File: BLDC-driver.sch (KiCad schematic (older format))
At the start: 103 parts, among them J1 Conn_01x06, J2 Conn_01x06, Q1 FDMS8018, Q2 FDMS8018, Q3 FDMS8018, Q4 FDMS8018, Q5 FDMS8018, Q6 FDMS8018, Q7 BC807, U1 NCP81151B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

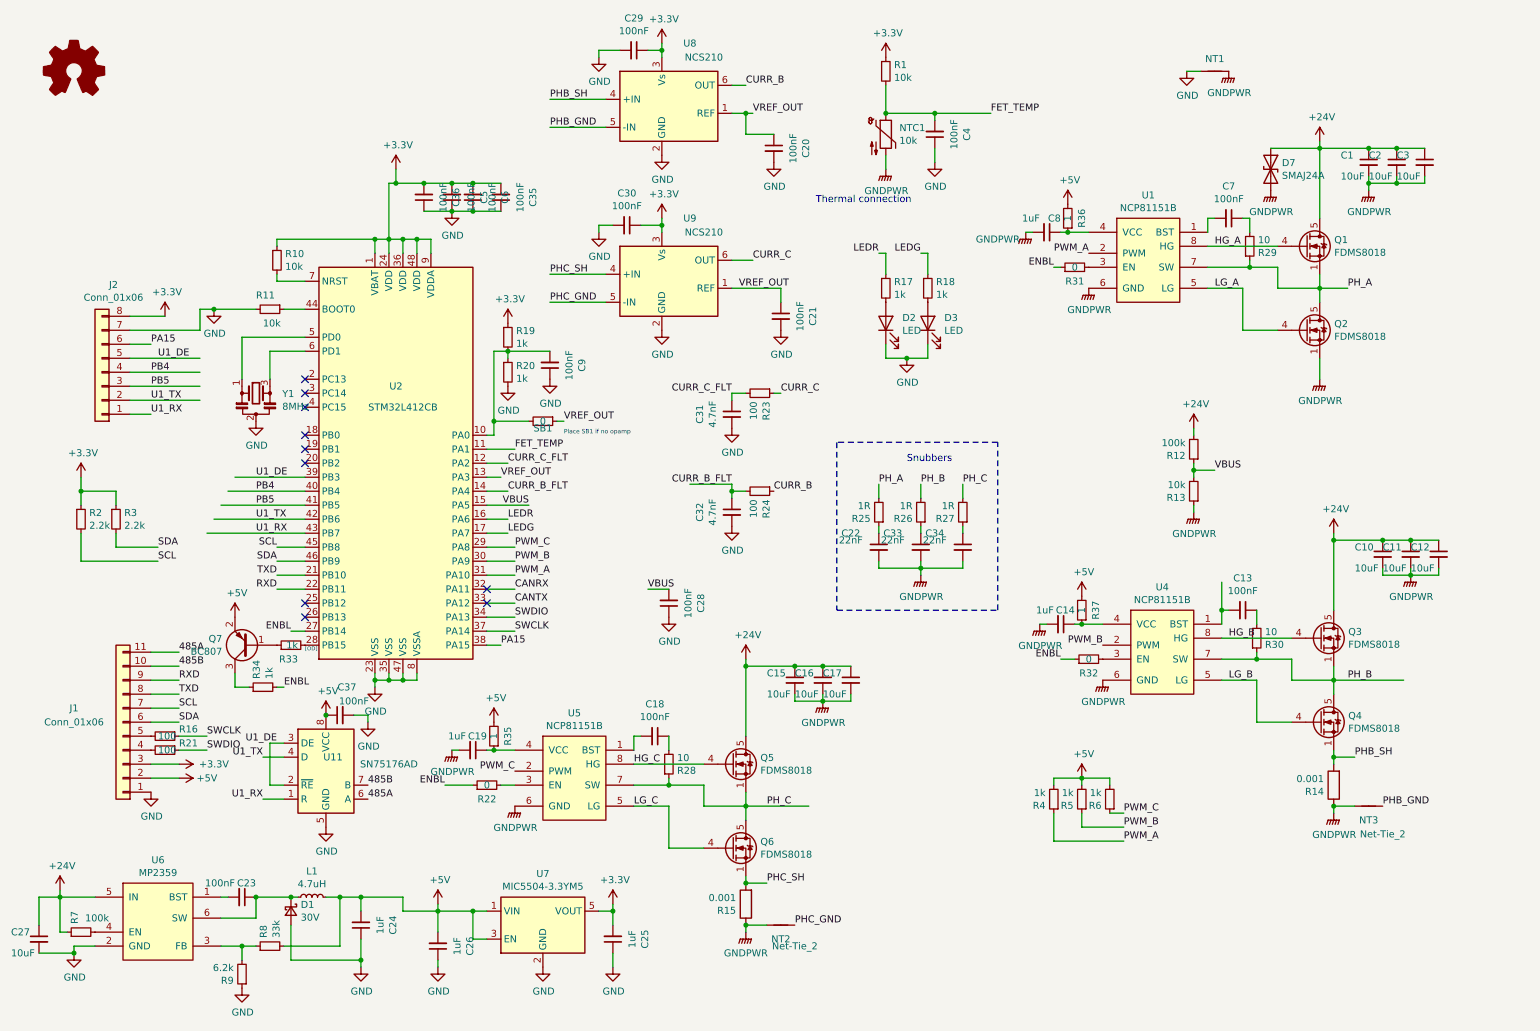
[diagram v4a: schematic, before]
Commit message: Multiple updates:
Change amp filter caps to 1nF
Move second shunt resistor to top layer
Make one hole grounded
various routing updates
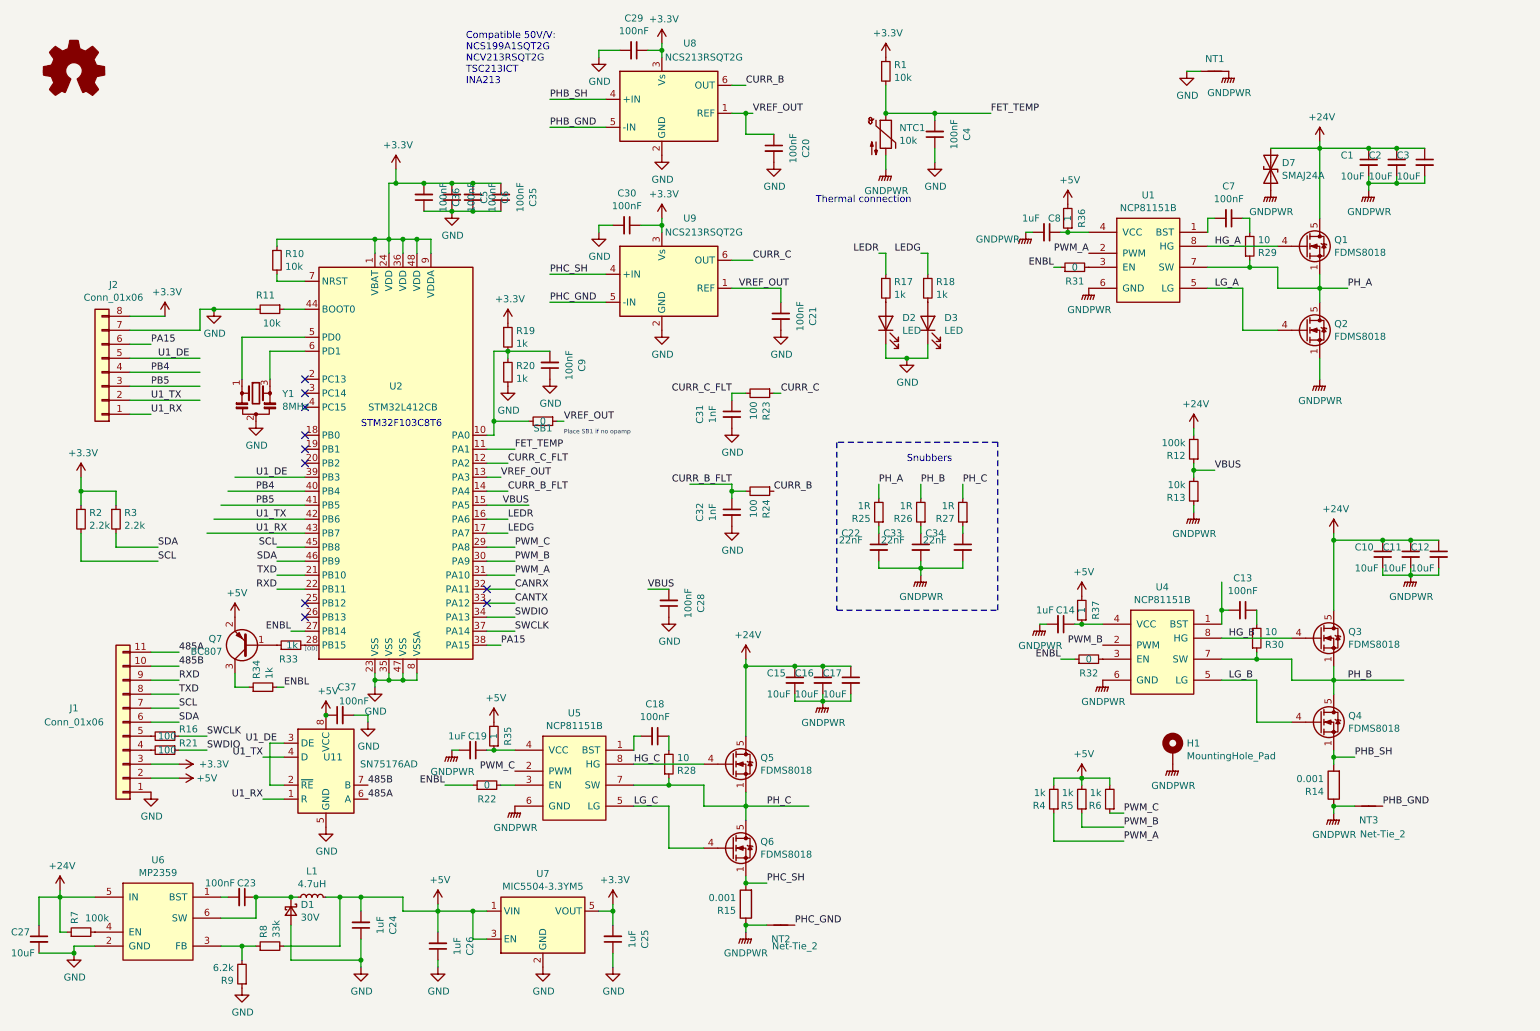
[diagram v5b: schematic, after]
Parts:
- added H1: MountingHole_Pad, MountingHole:MountingHole_3.2mm_M3_DIN965_Pad, symbol Mechanical:MountingHole_Pad
- C31, C32: value 4.7nF -> 1nF; JLCSMT C1538 -> C1523
- R14, R15: JLCSMT (none) -> C154629; JLCSMT_PKG (none) -> RES-SMD
- SB1: JLCSMT (none) -> C17168; JLCSMT_PKG (none) -> 0402
- U8, U9: value NCS210 -> NCS213RSQT2G
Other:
- note added: "Compatible 50V/V:\nNCS199A1SQT2G\nNCV213RSQT2G\nTSC213ICT\nINA213"
- note added: "STM32F103C8T6"
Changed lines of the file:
@@
 P 5100 1250
 F 0 "U8" H 5300 1750 50  0000 C CNN
-F 1 "NCS210" H 5400 1650 50  0000 C CNN
+F 1 "NCS213RSQT2G" H 5400 1650 50  0000 C CNN
 F 2 "Package_TO_SOT_SMD:SOT-363_SC-70-6" H 5100 1250 50  0001 C CNN
 F 3 "https://www.onsemi.com/pub/Collateral/NCS210R-D.PDF" H 5100 1250 50  0001 C CNN
@@
 F 4 "PMR25HZPFV1L00" H 9900 6050 50  0001 C CNN "MPN"
 F 5 "https://lt.farnell.com/rohm/pmr25hzpfv1l00/current-sense-res-0r001-1-1-w/dp/2696414" H 9900 6050 50  0001 C CNN "URL"
+F 6 "C154629" H 9900 6050 50  0001 C CNN "JLCSMT"
+F 7 "RES-SMD" H 9900 6050 50  0001 C CNN "JLCSMT_PKG"
 	1    9900 6050
 	-1   0    0    1
@@
 F 4 "PMR25HZPFV1L00" H 5700 6900 50  0001 C CNN "MPN"
 F 5 "https://lt.farnell.com/rohm/pmr25hzpfv1l00/current-sense-res-0r001-1-1-w/dp/2696414" H 5700 6900 50  0001 C CNN "URL"
+F 6 "C154629" H 5700 6900 50  0001 C CNN "JLCSMT"
+F 7 "RES-SMD" H 5700 6900 50  0001 C CNN "JLCSMT_PKG"
 	1    5700 6900
 	-1   0    0    1
@@
 P 5600 3400
 F 0 "C31" V 5371 3400 50  0000 C CNN
-F 1 "4.7nF" V 5462 3400 50  0000 C CNN
+F 1 "1nF" V 5462 3400 50  0000 C CNN
 F 2 "Capacitor_SMD:C_0402_1005Metric" H 5600 3400 50  0001 C CNN
 F 3 "~" H 5600 3400 50  0001 C CNN
-F 4 "C1538" H 5600 3400 50  0001 C CNN "JLCSMT"
+F 4 "C1523" H 5600 3400 50  0001 C CNN "JLCSMT"
 F 5 "0402" H 5600 3400 50  0001 C CNN "JLCSMT_PKG"
 	1    5600 3400
@@
 P 5600 4100
 F 0 "C32" V 5371 4100 50  0000 C CNN
-F 1 "4.7nF" V 5462 4100 50  0000 C CNN
+F 1 "1nF" V 5462 4100 50  0000 C CNN
 F 2 "Capacitor_SMD:C_0402_1005Metric" H 5600 4100 50  0001 C CNN
 F 3 "~" H 5600 4100 50  0001 C CNN
-F 4 "C1538" H 5600 4100 50  0001 C CNN "JLCSMT"
+F 4 "C1523" H 5600 4100 50  0001 C CNN "JLCSMT"
 F 5 "0402" H 5600 4100 50  0001 C CNN "JLCSMT_PKG"
 	1    5600 4100
@@
 P 5100 2500
 F 0 "U9" H 5300 3000 50  0000 C CNN
-F 1 "NCS210" H 5400 2900 50  0000 C CNN
+F 1 "NCS213RSQT2G" H 5400 2900 50  0000 C CNN
 F 2 "Package_TO_SOT_SMD:SOT-363_SC-70-6" H 5100 2500 50  0001 C CNN
 F 3 "https://www.onsemi.com/pub/Collateral/NCS210R-D.PDF" H 5100 2500 50  0001 C CNN
@@
 F 2 "Resistor_SMD:R_0402_1005Metric" H 4250 3450 50  0001 C CNN
 F 3 "~" H 4250 3450 50  0001 C CNN
+F 4 "C17168" H 4250 3450 50  0001 C CNN "JLCSMT"
+F 5 "0402" H 4250 3450 50  0001 C CNN "JLCSMT_PKG"
 	1    4250 3450
 	0    1    1    0
@@
 NoConn ~ 2550 4750
 NoConn ~ 2550 4850
+Text Notes 3700 1050 0    50   ~ 0
+Compatible 50V/V:\nNCS199A1SQT2G\nNCV213RSQT2G\nTSC213ICT\nINA213
+Text Notes 2950 3500 0    50   ~ 0
+STM32F103C8T6
+$Comp
+L Mechanical:MountingHole_Pad H1
+U 1 1 60F815C2
+P 8750 5800
+F 0 "H1" H 8850 5849 50  0000 L CNN
+F 1 "MountingHole_Pad" H 8850 5758 50  0000 L CNN
+F 2 "MountingHole:MountingHole_3.2mm_M3_DIN965_Pad" H 8750 5800 50  0001 C CNN
+F 3 "~" H 8750 5800 50  0001 C CNN
+	1    8750 5800
+	1    0    0    -1
+$EndComp
+$Comp
+L power:GNDPWR #PWR0130
+U 1 1 60F81DE6
+P 8750 5900
+F 0 "#PWR0130" H 8750 5700 50  0001 C CNN
+F 1 "GNDPWR" H 8754 5746 50  0000 C CNN
+F 2 "" H 8750 5850 50  0001 C CNN
+F 3 "" H 8750 5850 50  0001 C CNN
+	1    8750 5900
+	1    0    0    -1
+$EndComp
 $EndSCHEMATC

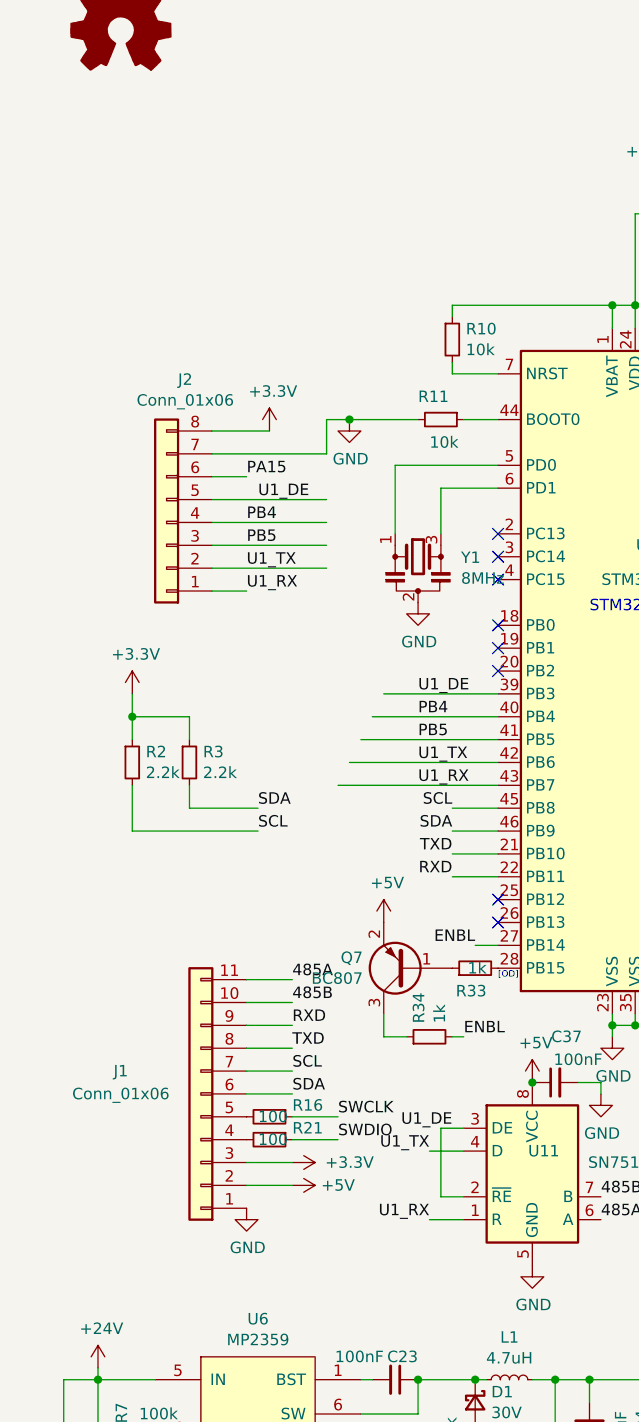
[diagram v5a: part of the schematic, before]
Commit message: Rev3: Update connectors, add JST PH connectors
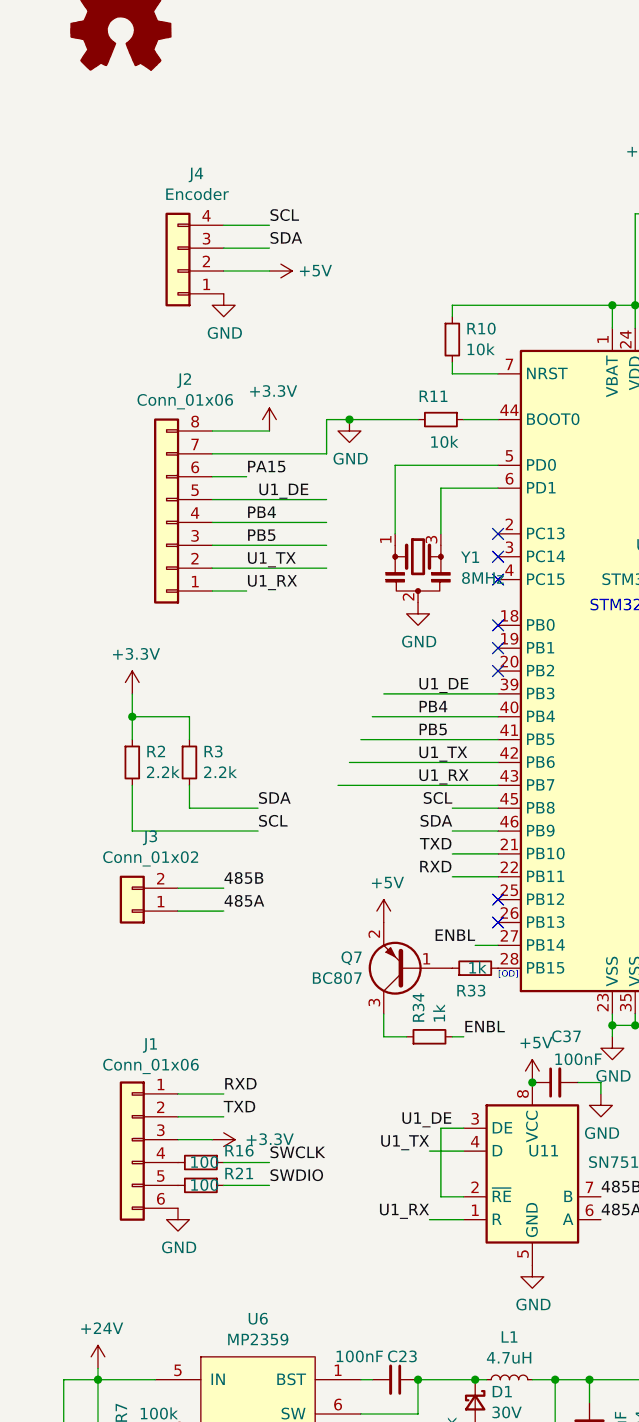
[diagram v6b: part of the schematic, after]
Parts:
- removed J1: Conn_01x06, Connector_PinHeader_2.00mm:PinHeader_1x11_P2.00mm_Vertical, symbol Connector_Generic:Conn_01x11
- added J1: Conn_01x06, Connector_JST:JST_PH_S6B-PH-K_1x06_P2.00mm_Horizontal, symbol Connector_Generic:Conn_01x06
- added J3: Conn_01x02, Connector_JST:JST_PH_S2B-PH-K_1x02_P2.00mm_Horizontal, symbol Connector_Generic:Conn_01x02
- added J4: Encoder, Connector_PinSocket_2.00mm:PinSocket_1x04_P2.00mm_Vertical, symbol Connector_Generic:Conn_01x04
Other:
- moved on the sheet: R16, R21
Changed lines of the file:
@@
 Wire Wire Line
 	3850 3550 3900 3550
-Text Label 1650 5300 0    50   ~ 0
+Text Label 1350 5600 0    50   ~ 0
 RXD
-Text Label 1650 5400 0    50   ~ 0
+Text Label 1350 5700 0    50   ~ 0
 TXD
 Wire Wire Line
-	1650 5400 1450 5400
-Wire Wire Line
-	1450 5300 1650 5300
-Text Label 1650 5500 0    50   ~ 0
+	1350 5700 1150 5700
+Wire Wire Line
+	1150 5600 1350 5600
+Text Label 1550 1800 0    50   ~ 0
 SCL
-Text Label 1650 5600 0    50   ~ 0
+Text Label 1550 1900 0    50   ~ 0
 SDA
 Wire Wire Line
-	1650 5500 1450 5500
-Wire Wire Line
-	1450 5600 1650 5600
-Text Label 1850 5700 0    50   ~ 0
+	1550 1800 1350 1800
+Wire Wire Line
+	1350 1900 1550 1900
+Text Label 1550 5900 0    50   ~ 0
 SWCLK
-Text Label 1850 5800 0    50   ~ 0
+Text Label 1550 6000 0    50   ~ 0
 SWDIO
 Wire Wire Line
-	1850 5700 1650 5700
-Wire Wire Line
-	1650 5800 1850 5800
+	1550 5900 1350 5900
 $Comp
 L power:GND #PWR034
 U 1 1 5F120A4B
-P 1450 6100
-F 0 "#PWR034" H 1450 5850 50  0001 C CNN
-F 1 "GND" H 1455 5927 50  0000 C CNN
-F 2 "" H 1450 6100 50  0001 C CNN
-F 3 "" H 1450 6100 50  0001 C CNN
-	1    1450 6100
+P 1150 6100
+F 0 "#PWR034" H 1150 5850 50  0001 C CNN
+F 1 "GND" H 1155 5927 50  0000 C CNN
+F 2 "" H 1150 6100 50  0001 C CNN
+F 3 "" H 1150 6100 50  0001 C CNN
+	1    1150 6100
 	1    0    0    -1
 $EndComp
@@
 L power:+5V #PWR032
 U 1 1 5EEDF35F
-P 1650 6000
-F 0 "#PWR032" H 1650 5850 50  0001 C CNN
-F 1 "+5V" V 1650 6200 50  0000 C CNN
-F 2 "" H 1650 6000 50  0001 C CNN
-F 3 "" H 1650 6000 50  0001 C CNN
-	1    1650 6000
+P 1550 2000
+F 0 "#PWR032" H 1550 1850 50  0001 C CNN
+F 1 "+5V" V 1550 2200 50  0000 C CNN
+F 2 "" H 1550 2000 50  0001 C CNN
+F 3 "" H 1550 2000 50  0001 C CNN
+	1    1550 2000
 	0    1    1    0
 $EndComp
 Wire Wire Line
-	1650 6000 1450 6000
+	1550 2000 1350 2000
 $Comp
 L power:GND #PWR046
@@
 L power:+3.3V #PWR0109
 U 1 1 5F9E74A9
-P 1650 5900
-F 0 "#PWR0109" H 1650 5750 50  0001 C CNN
-F 1 "+3.3V" V 1650 6150 50  0000 C CNN
-F 2 "" H 1650 5900 50  0001 C CNN
-F 3 "" H 1650 5900 50  0001 C CNN
-	1    1650 5900
+P 1300 5800
+F 0 "#PWR0109" H 1300 5650 50  0001 C CNN
+F 1 "+3.3V" V 1300 6050 50  0000 C CNN
+F 2 "" H 1300 5800 50  0001 C CNN
+F 3 "" H 1300 5800 50  0001 C CNN
+	1    1300 5800
 	0    1    1    0
 $EndComp
-Wire Wire Line
-	1650 5900 1450 5900
-Text Label 1650 5100 0    50   ~ 0
+Text Label 1350 4800 0    50   ~ 0
 485A
 Wire Wire Line
-	1650 5100 1450 5100
-Text Label 1650 5200 0    50   ~ 0
+	1350 4800 1150 4800
+Text Label 1350 4700 0    50   ~ 0
 485B
 Wire Wire Line
-	1650 5200 1450 5200
+	1350 4700 1150 4700
 Text Notes 6200 1900 0    50   ~ 0
 Thermal connection
@@
 $EndComp
 $Comp
-L Connector_Generic:Conn_01x11 J1
-U 1 1 5F108F52
-P 1250 5600
-F 0 "J1" H 1600 5500 50  0000 C CNN
-F 1 "Conn_01x06" H 1600 5600 50  0000 C CNN
-F 2 "Connector_PinHeader_2.00mm:PinHeader_1x11_P2.00mm_Vertical" H 1250 5600 50  0001 C CNN
-F 3 "~" H 1250 5600 50  0001 C CNN
-	1    1250 5600
-	-1   0    0    1
-$EndComp
-$Comp
 L Regulator_Linear:MIC5504-3.3YM5 U7
 U 1 1 5EEEC834
@@
 L Device:R_Small R16
 U 1 1 60B85EAE
-P 1550 5700
-F 0 "R16" V 1500 5800 50  0000 L CNN
-F 1 "100" V 1550 5650 50  0000 L CNN
-F 2 "Resistor_SMD:R_0402_1005Metric" H 1550 5700 50  0001 C CNN
-F 3 "~" H 1550 5700 50  0001 C CNN
-F 4 "0402" H 1550 5700 50  0001 C CNN "JLCSMT_PKG"
-F 5 "C25076" H 1550 5700 50  0001 C CNN "JLCSMT"
-	1    1550 5700
+P 1250 5900
+F 0 "R16" V 1200 6000 50  0000 L CNN
+F 1 "100" V 1250 5850 50  0000 L CNN
+F 2 "Resistor_SMD:R_0402_1005Metric" H 1250 5900 50  0001 C CNN
+F 3 "~" H 1250 5900 50  0001 C CNN
+F 4 "0402" H 1250 5900 50  0001 C CNN "JLCSMT_PKG"
+F 5 "C25076" H 1250 5900 50  0001 C CNN "JLCSMT"
+	1    1250 5900
 	0    1    1    0
 $EndComp
@@
 L Device:R_Small R21
 U 1 1 60BC204F
-P 1550 5800
-F 0 "R21" V 1500 5900 50  0000 L CNN
-F 1 "100" V 1550 5750 50  0000 L CNN
-F 2 "Resistor_SMD:R_0402_1005Metric" H 1550 5800 50  0001 C CNN
-F 3 "~" H 1550 5800 50  0001 C CNN
-F 4 "0402" H 1550 5800 50  0001 C CNN "JLCSMT_PKG"
-F 5 "C25076" H 1550 5800 50  0001 C CNN "JLCSMT"
-	1    1550 5800
+P 1250 6000
+F 0 "R21" V 1200 6100 50  0000 L CNN
+F 1 "100" V 1250 5950 50  0000 L CNN
+F 2 "Resistor_SMD:R_0402_1005Metric" H 1250 6000 50  0001 C CNN
+F 3 "~" H 1250 6000 50  0001 C CNN
+F 4 "0402" H 1250 6000 50  0001 C CNN "JLCSMT_PKG"
+F 5 "C25076" H 1250 6000 50  0001 C CNN "JLCSMT"
+	1    1250 6000
 	0    1    1    0
 $EndComp
@@
 	1    0    0    -1
 $EndComp
+Wire Wire Line
+	1350 6000 1550 6000
+Wire Wire Line
+	1300 5800 1150 5800
+$Comp
+L Connector_Generic:Conn_01x02 J3
+U 1 1 61170D86
+P 950 4800
+F 0 "J3" H 868 4475 50  0000 C CNN
+F 1 "Conn_01x02" H 868 4566 50  0000 C CNN
+F 2 "Connector_JST:JST_PH_S2B-PH-K_1x02_P2.00mm_Horizontal" H 950 4800 50  0001 C CNN
+F 3 "~" H 950 4800 50  0001 C CNN
+	1    950  4800
+	-1   0    0    1
+$EndComp
+$Comp
+L power:GND #PWR0131
+U 1 1 6124CC7D
+P 1350 2100
+F 0 "#PWR0131" H 1350 1850 50  0001 C CNN
+F 1 "GND" H 1355 1927 50  0000 C CNN
+F 2 "" H 1350 2100 50  0001 C CNN
+F 3 "" H 1350 2100 50  0001 C CNN
+	1    1350 2100
+	1    0    0    -1
+$EndComp
+$Comp
+L Connector_Generic:Conn_01x06 J1
+U 1 1 612ABD87
+P 950 5800
+F 0 "J1" H 868 6217 50  0000 C CNN
+F 1 "Conn_01x06" H 868 6126 50  0000 C CNN
+F 2 "Connector_JST:JST_PH_S6B-PH-K_1x06_P2.00mm_Horizontal" H 950 5800 50  0001 C CNN
+F 3 "~" H 950 5800 50  0001 C CNN
+	1    950  5800
+	-1   0    0    -1
+$EndComp
+$Comp
+L Connector_Generic:Conn_01x04 J4
+U 1 1 61312986
+P 1150 2000
+F 0 "J4" H 1068 1575 50  0000 C CNN
+F 1 "Encoder" H 1068 1666 50  0000 C CNN
+F 2 "Connector_PinSocket_2.00mm:PinSocket_1x04_P2.00mm_Vertical" H 1150 2000 50  0001 C CNN
+F 3 "~" H 1150 2000 50  0001 C CNN
+	1    1150 2000
+	-1   0    0    1
+$EndComp
 $EndSCHEMATC
